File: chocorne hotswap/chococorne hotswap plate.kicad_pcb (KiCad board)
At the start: 2 copper layers, 130 x 87.7 mm, 29 parts, among them SW1 SW_PUSH, SW10 SW_PUSH, SW11 SW_PUSH, SW12 SW_PUSH, SW13 SW_PUSH, SW14 SW_PUSH, SW15 SW_PUSH, SW16 SW_PUSH, SW17 SW_PUSH, SW18 SW_PUSH, SW19 SW_PUSH, SW2 SW_PUSH, SW20 SW_PUSH, SW21 SW_PUSH, SW3 SW_PUSH, SW4 SW_PUSH, SW5 SW_PUSH, SW6 SW_PUSH, SW7 SW_PUSH, SW8 SW_PUSH, SW9 SW_PUSH

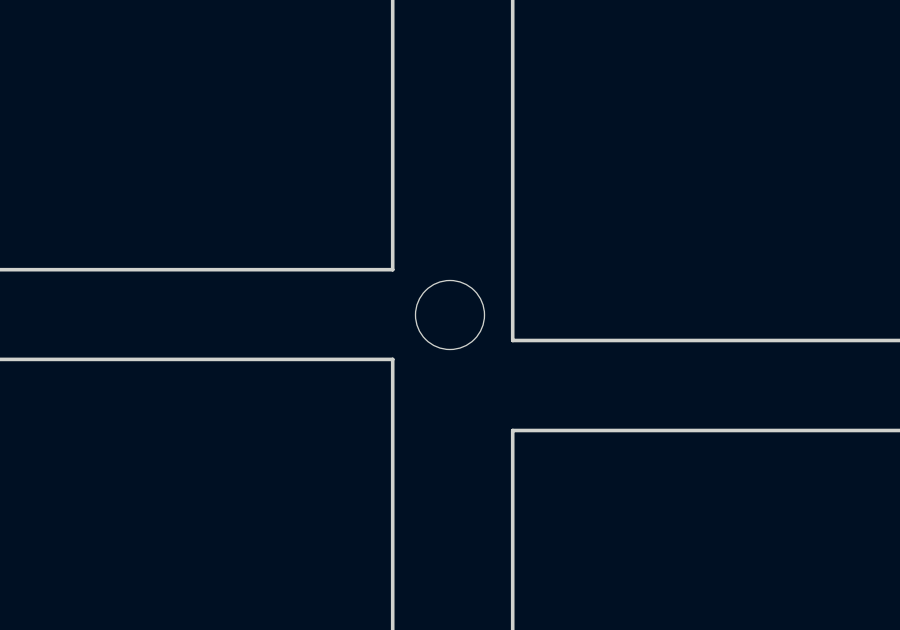
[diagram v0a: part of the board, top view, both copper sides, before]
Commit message: chocorne: remove one of the mounting holes that isn't used
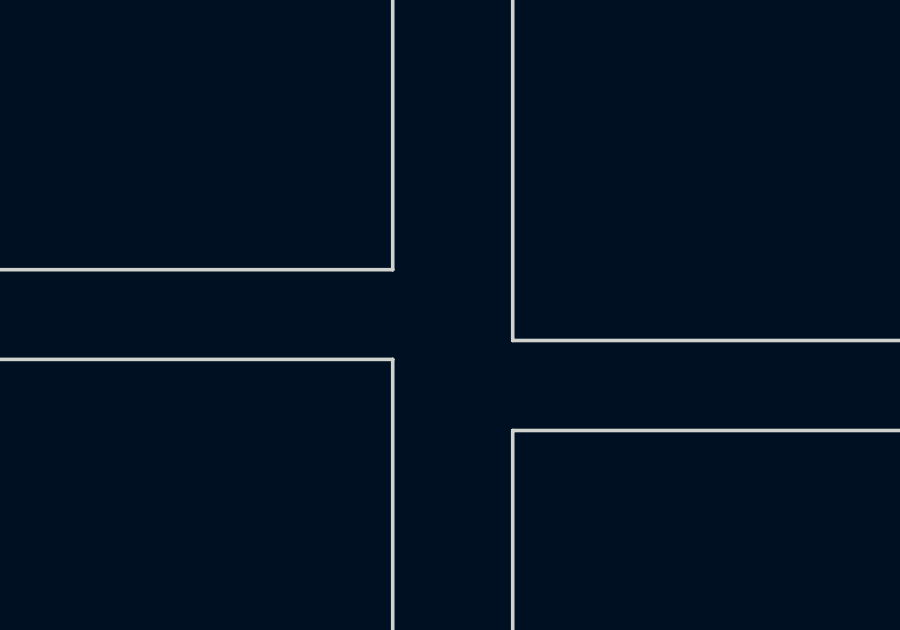
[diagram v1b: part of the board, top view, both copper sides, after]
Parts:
- removed ?: M2_HOLE_NPH, holykeebs:M2_HOLE_NPH
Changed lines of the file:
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@@
       (stroke (width 0.15) (type solid)) (layer "F.Fab"))
-  )
-  (footprint "holykeebs:M2_HOLE_NPH" (layer "F.Cu")
-    (at 223.722 69.7)
-    (attr through_hole)
-    (fp_text reference "" (at 0 -0.5 unlocked) (layer "F.SilkS") hide
-        (effects (font (size 1 1) (thickness 0.1)))
-    )
-    (fp_text value "M2_HOLE_NPH" (at 0 1 unlocked) (layer "F.Fab") hide
-        (effects (font (size 1 1) (thickness 0.15)))
-    )
-    (fp_text user "${REFERENCE}" (at 0.3 0) (layer "F.Fab") hide
-        (effects (font (size 1 1) (thickness 0.15)))
-    )
-    (pad "" np_thru_hole circle (at 0 0) (size 2.3 2.3) (drill 2.3) (layers "F&B.Cu" "*.Mask"))
   )
   (footprint "kbd:SW_Hole" (layer "F.Cu")
@@
       )
       (stroke (width 0.01) (type solid)) (fill solid) (layer "B.Mask"))
-    (group "" (id f649217c-c27c-4a41-8167-4a44b386c6de)
-      (members
-        090547b1-2640-4255-9ae1-98b142660245
-        484f7b7b-26b6-4cee-bfbf-a3770693b14a
-        55ce9735-e7d3-49ae-b408-51e17cb86c1c
-        596308fc-583d-4604-a789-f37626c2c4d1
-        646dfad1-d5bd-4161-840d-71bb190f300e
-        c79296db-67e3-47eb-9f93-b0497aa61888
-      )
-    )
   )
   (gr_line (start 148.859294 117.98231) (end 160.7725 138.58)

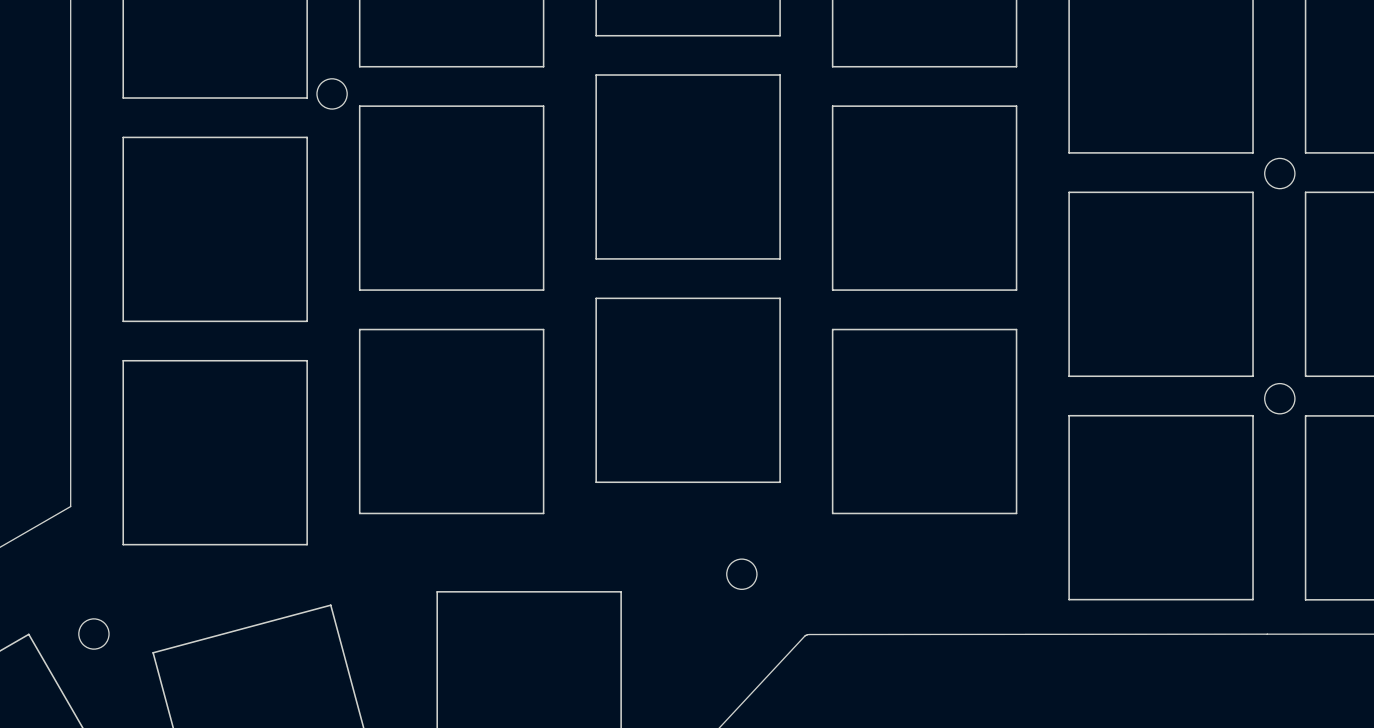
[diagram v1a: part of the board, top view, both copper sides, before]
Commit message: chocorne: move holes to m2 spacers footprint
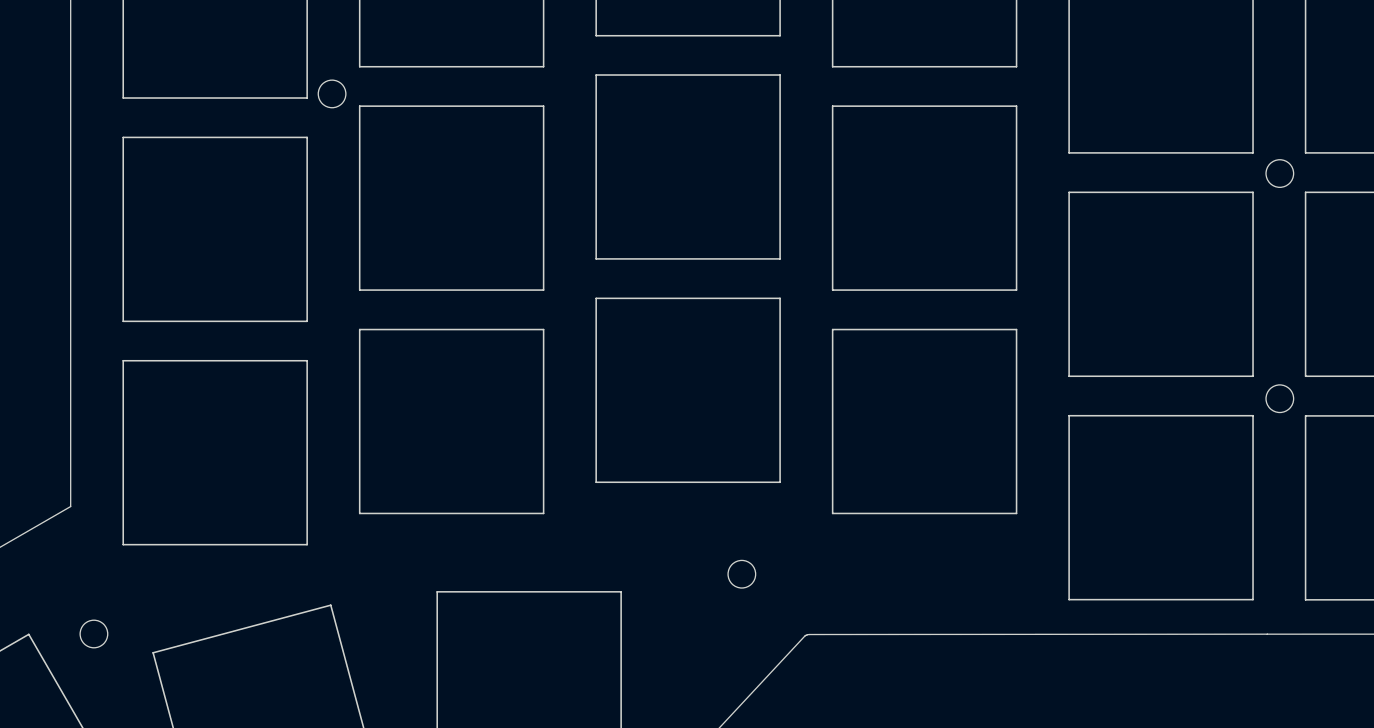
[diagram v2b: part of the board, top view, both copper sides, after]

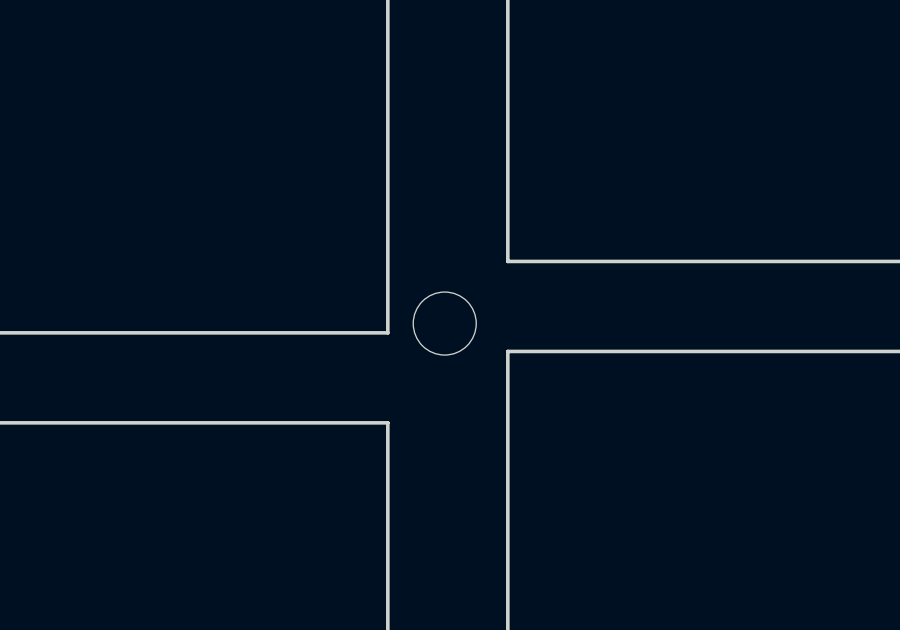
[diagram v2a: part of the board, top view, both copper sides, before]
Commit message: chocorne: move top right mounting hole so screw head doesn't hit the switch edge
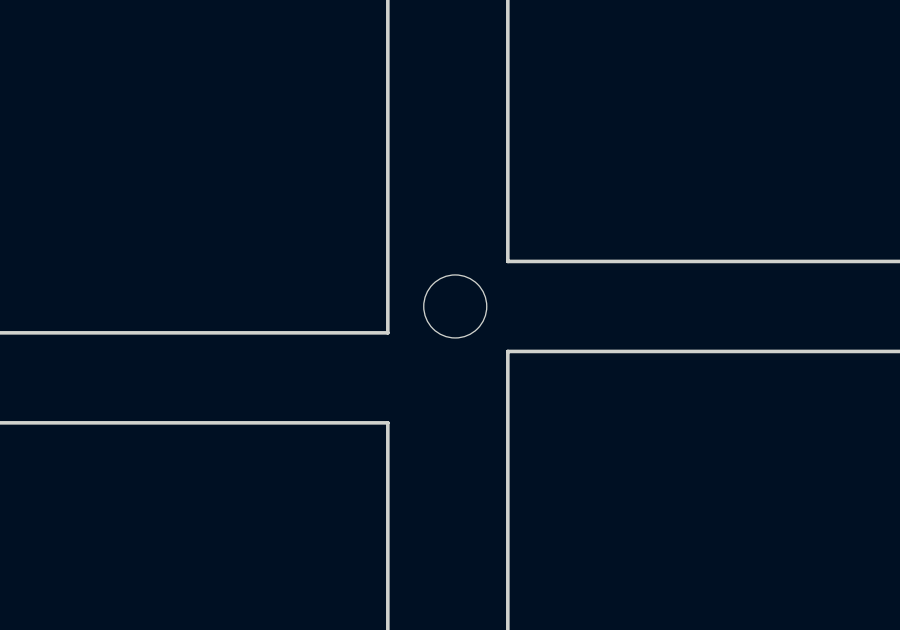
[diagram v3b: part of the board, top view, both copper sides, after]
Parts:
- removed REF**: M2_HOLE_NPH, holykeebs:M2_HOLE_NPH
- added ?: M2_HOLE_NPH, holykeebs:M2_HOLE_NPH, F.Cu at (188.1, 72.0)
